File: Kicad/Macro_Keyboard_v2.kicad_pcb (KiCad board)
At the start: 2 copper layers, 171 x 92 mm, 98 parts, among them J1 Conn_01x04_Female, SW1 RESET SWITCH, SW10 SW_Push, SW11 SW_Push, SW12 SW_Push, SW13 SW_Push, SW14 SW_Push, SW15 SW_Push, SW16 SW_Push, SW17 SW_Push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

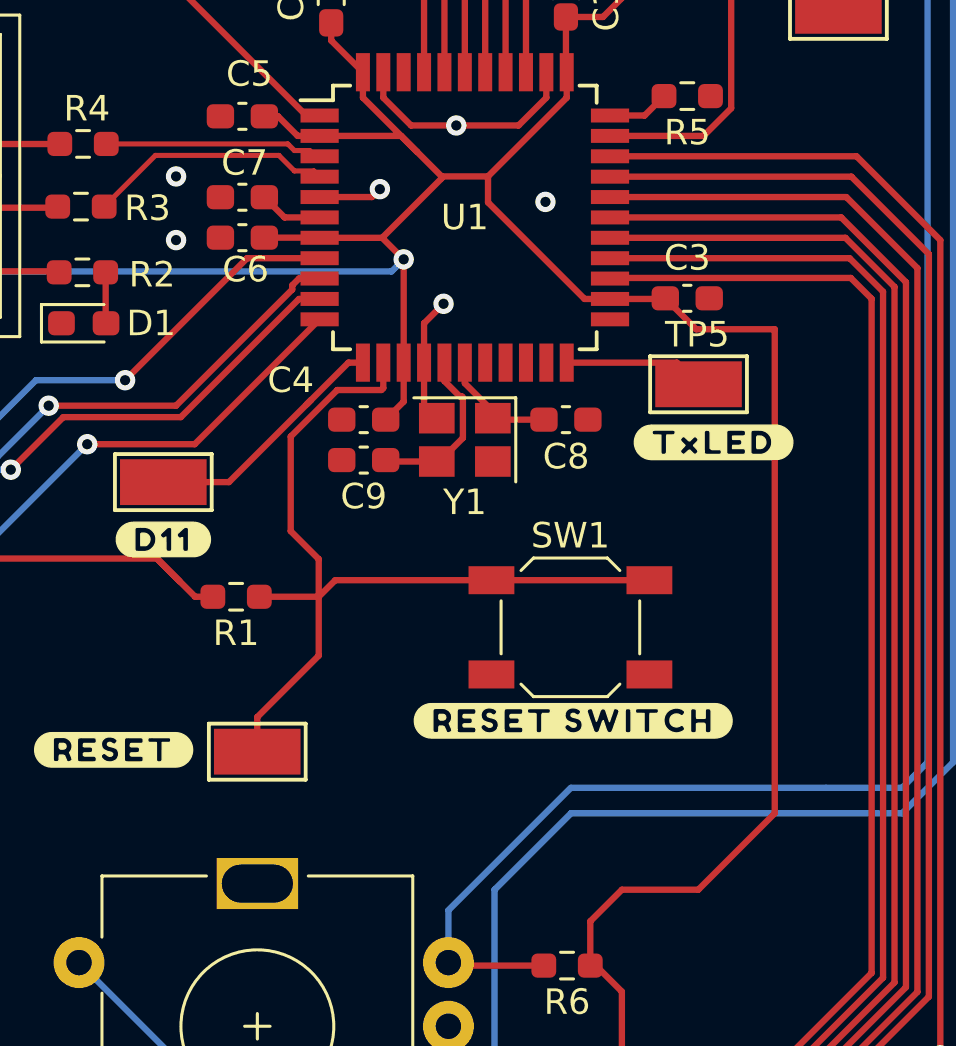
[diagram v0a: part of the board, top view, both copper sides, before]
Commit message: little silkscreen update
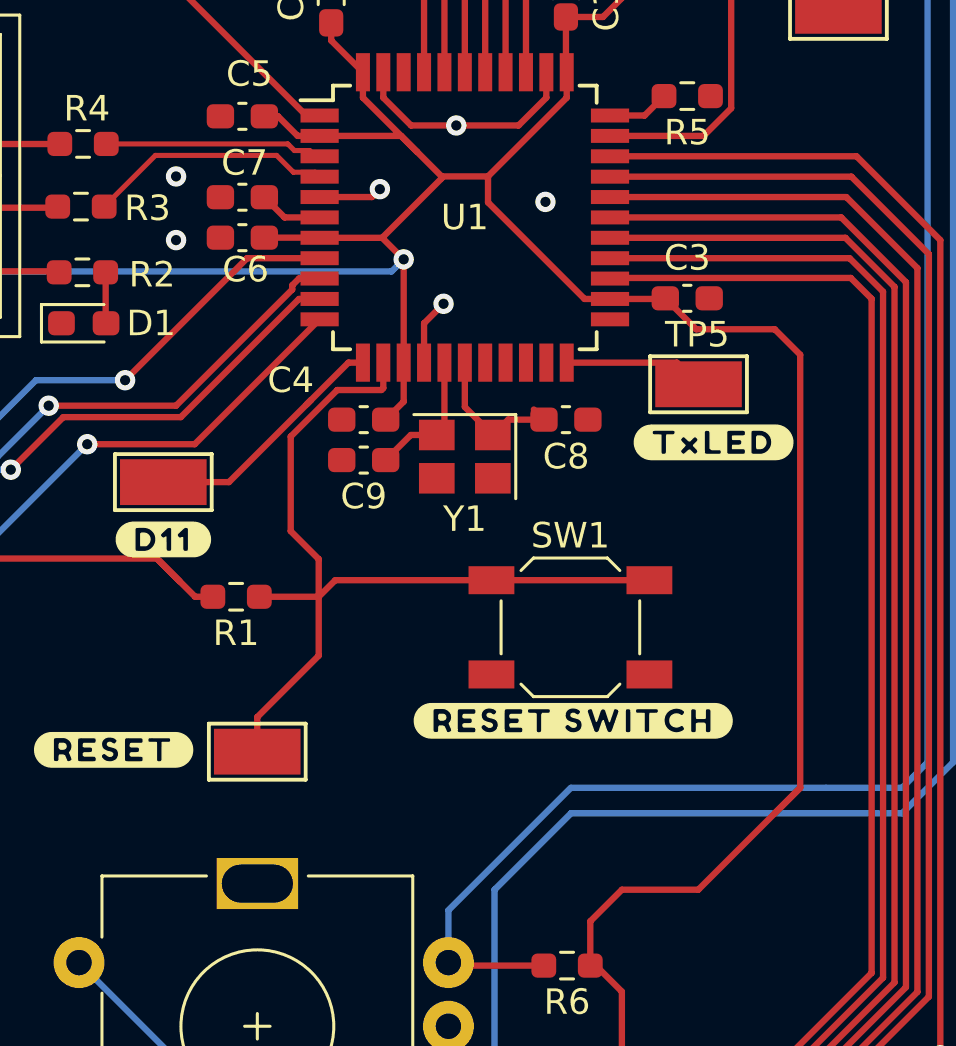
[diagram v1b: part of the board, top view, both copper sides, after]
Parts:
- C2, C3, C4, C5: value 0.1uF -> 100nF
- Y1: value 16MHz -> Crystal
- moved Y1 0.66 mm to (215.8, 107.0)
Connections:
- Y1 pad 2: GND -> Net-(C9-Pad1)
- Y1 pad 3: Net-(C9-Pad1) -> (no net)
- Y1 pad 4: GND -> (no net)
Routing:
- net GND: track 35.5 -> 33.1 mm
- net VCC: track 169.4 -> 171.6 mm
- net Net-(C8-Pad1): track 4.67 -> 6.11 mm
- net Net-(C9-Pad1): track 6.74 -> 5.46 mm
